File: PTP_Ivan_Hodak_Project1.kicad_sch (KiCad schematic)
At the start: 0 parts

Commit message: ispunjena sastavnica
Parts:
- added R1, R2: R_Small, symbol Device:R_Small
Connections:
- new net +3.3V: R2.1
- new net GND: R1.2
- new net U_izl: R1.1, R2.2
- no-connect marks 0 -> 1
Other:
- company: (none) -> TVZ
- title: (none) -> BCD Brojač

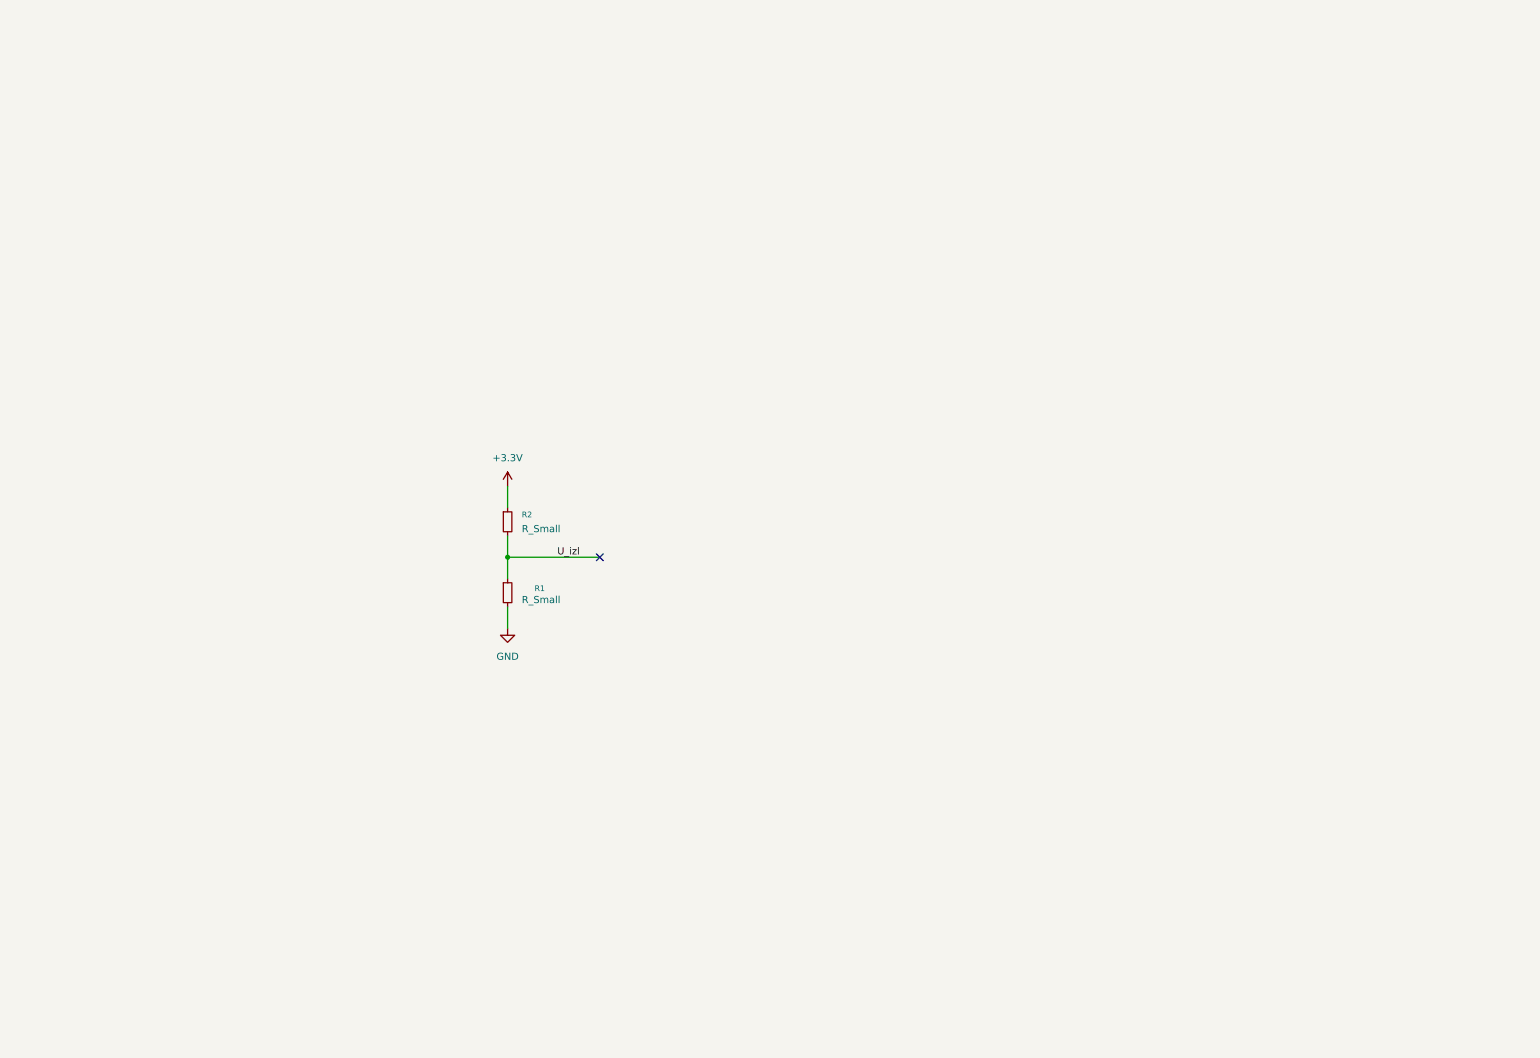
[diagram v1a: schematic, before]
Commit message: Dodali komponente
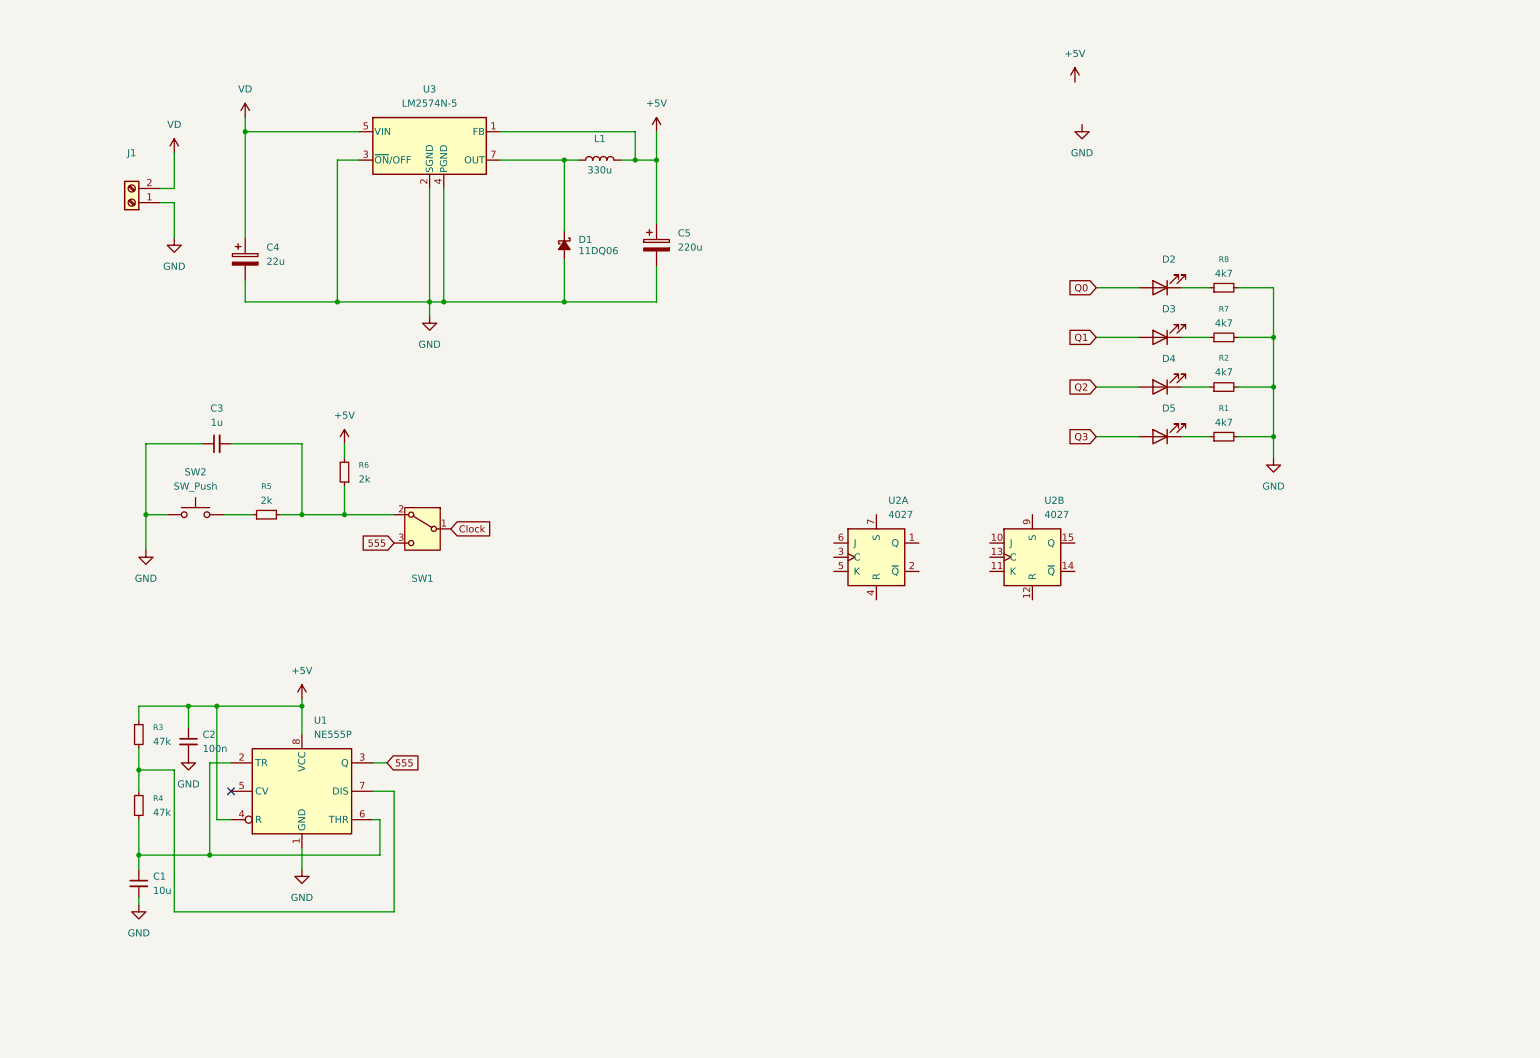
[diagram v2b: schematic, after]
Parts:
- added C1: 10u, symbol Device:C_Small
- added C2: 100n, symbol Device:C_Small
- added C3: 1u, symbol Device:C_Small
- added C4: 22u, symbol Device:C_Polarized
- added C5: 220u, symbol Device:C_Polarized
- added D1: 11DQ06, symbol Device:D_Schottky_Small_Filled
- added D2, D3, D4, D5: LED, symbol Device:LED
- added J1: ~, symbol Connector:Screw_Terminal_01x02
- added L1: 330u, symbol Device:L
- added R3, R4: 47k, symbol Device:R_Small
- added R5, R6: 2k, symbol Device:R_Small
- added R7, R8: 4k7, symbol Device:R_Small
- added SW1: SW_SPDT, symbol Switch:SW_SPDT
- added SW2: SW_Push, symbol Switch:SW_Push
- added U1: NE555P, Package_DIP:DIP-8_W7.62mm, symbol Timer:NE555P
- added U2: 4027, symbol 4xxx:4027
- added U3: LM2574N-5, Package_DIP:DIP-8_W7.62mm, symbol Regulator_Switching:LM2574N-5
- R1, R2: value R_Small -> 4k7
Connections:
- net GND: now also R2.2, C1.2, C2.2, C3.1, C4.2, C5.2, D1.2 (A), J1.1 (Pin_1), R7.2, R8.2, SW2.1, U1.1 (GND), U3.2 (SGND), U3.3 (~{ON}/OFF), U3.4 (PGND)
- net +3.3V: no longer names the net of R2.1
- net +3.3V: now also D4.1 (K)
- net U_izl: no longer names the net of R1.1
- net U_izl: now also D5.1 (K); no longer R2.2
- new net: C3.2, R5.2, R6.1, SW1.2 (B)
- new net: D1.1 (K), L1.1, U3.7 (OUT)
- new net: C1.1, R4.2, U1.2 (TR), U1.6 (THR)
- new net: R3.2, R4.1, U1.7 (DIS)
- new net: D3.1 (K), R7.1
- new net: D2.1 (K), R8.1
- new net: R5.1, SW2.2
- new net +5V: C2.1, C5.1, L1.2, R3.1, R6.2, U1.4 (R), U1.8 (VCC), U3.1 (FB)
- new net 555: SW1.3 (C), U1.3 (Q)
- new net Clock: SW1.1 (A)
- new net Q0: D2.2 (A)
- new net Q1: D3.2 (A)
- new net Q2: D4.2 (A)
- new net Q3: D5.2 (A)
- new net VD: C4.1, J1.2 (Pin_2), U3.5 (VIN)

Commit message: LV3
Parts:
- added U6: 74LVC1G11, SOT23-6:SOT-23-6, symbol SN74LVC1G11:SN74LVC1G11
- renumbered R5 to R13, R6 to R7, SW2 to SW1, SW1 to SW2
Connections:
- net +5V: now also U6.5 (Vcc)
- net Clock: now also R7.1, U6.3 (B)
- net GND: now also U6.2 (GND)
- net Q1: now also U6.6 (C)
- net Q3: now also U6.1 (A)
- net at C3.2, R13.2, SW2.2 (B): no longer R7.1
- new net Reset: U6.4 (Y)
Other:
- moved on the sheet: R7, SW2

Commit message: LV3 overwrite
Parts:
- R7: value 2k -> 10k
- renumbered C4 to C1, C5 to C2, D2 to D1, D3 to D2, D4 to D3, D1 to D4, R8 to R1, R7 to R2, R2 to R3, R1 to R4, U3 to U1
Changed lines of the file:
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@@
 			)
 		)
-		(property "Value" "2k"
+		(property "Value" "10k"
 			(at 88.9 100.3299 0)
 			(effects
@@
 		(on_board yes)
 		(dnp no)
-		(property "Reference" "D1"
+		(property "Reference" "D4"
 			(at 114.3 54.3559 90)
 			(effects
@@
 			(project ""
 				(path "/27044ca4-d0f9-45b4-abc4-d126f8e30ea6"
-					(reference "D1")
+					(reference "D4")
 					(unit 1)
 				)
@@
 		(dnp no)
 		(fields_autoplaced yes)
-		(property "Reference" "D4"
+		(property "Reference" "D3"
 			(at 220.0275 74.93 0)
 			(effects
@@
 			(project "PTP_Ivan_Hodak_Project1"
 				(path "/27044ca4-d0f9-45b4-abc4-d126f8e30ea6"
-					(reference "D4")
+					(reference "D3")
 					(unit 1)
 				)
@@
 		(dnp no)
 		(fields_autoplaced yes)
-		(property "Reference" "D3"
+		(property "Reference" "D2"
 			(at 220.0275 66.04 0)
 			(effects
@@
 			(project ""
 				(path "/27044ca4-d0f9-45b4-abc4-d126f8e30ea6"
-					(reference "D3")
+					(reference "D2")
 					(unit 1)
 				)
@@
 		(dnp no)
 		(fields_autoplaced yes)
-		(property "Reference" "D2"
+		(property "Reference" "D1"
 			(at 220.0275 57.15 0)
 			(effects
@@
 			(project ""
 				(path "/27044ca4-d0f9-45b4-abc4-d126f8e30ea6"
-					(reference "D2")
+					(reference "D1")
 					(unit 1)
 				)
@@
 		(dnp no)
 		(fields_autoplaced yes)
-		(property "Reference" "R2"
-			(at 229.87 74.8087 90)
+		(property "Reference" "R3"
+			(at 229.87 74.93 90)
 			(effects
 				(font
@@
 		)
 		(property "Value" "4k7"
-			(at 229.87 77.3487 90)
+			(at 229.87 77.47 90)
 			(effects
 				(font
@@
 			(project "PTP_Ivan_Hodak_Project1"
 				(path "/27044ca4-d0f9-45b4-abc4-d126f8e30ea6"
-					(reference "R2")
+					(reference "R3")
 					(unit 1)
 				)
@@
 		(dnp no)
 		(fields_autoplaced yes)
-		(property "Reference" "U3"
+		(property "Reference" "U1"
 			(at 87.63 26.67 0)
 			(effects
@@
 			(project ""
 				(path "/27044ca4-d0f9-45b4-abc4-d126f8e30ea6"
-					(reference "U3")
+					(reference "U1")
 					(unit 1)
 				)
@@
 		(dnp no)
 		(fields_autoplaced yes)
-		(property "Reference" "R1"
+		(property "Reference" "R4"
 			(at 229.87 83.82 90)
 			(effects
@@
 			(project ""
 				(path "/27044ca4-d0f9-45b4-abc4-d126f8e30ea6"
-					(reference "R1")
+					(reference "R4")
 					(unit 1)
 				)
@@
 		(dnp no)
 		(fields_autoplaced yes)
-		(property "Reference" "C5"
+		(property "Reference" "C2"
 			(at 132.08 52.4509 0)
 			(effects
@@
 			(project ""
 				(path "/27044ca4-d0f9-45b4-abc4-d126f8e30ea6"
-					(reference "C5")
+					(reference "C2")
 					(unit 1)
 				)
@@
 		(dnp no)
 		(fields_autoplaced yes)
-		(property "Reference" "R8"
+		(property "Reference" "R1"
 			(at 229.87 57.15 90)
 			(effects
@@
 			(project "PTP_Ivan_Hodak_Project1"
 				(path "/27044ca4-d0f9-45b4-abc4-d126f8e30ea6"
-					(reference "R8")
+					(reference "R1")
 					(unit 1)
 				)
@@
 		(dnp no)
 		(fields_autoplaced yes)
-		(property "Reference" "R7"
+		(property "Reference" "R2"
 			(at 229.87 66.04 90)
 			(effects
@@
 			(project "PTP_Ivan_Hodak_Project1"
 				(path "/27044ca4-d0f9-45b4-abc4-d126f8e30ea6"
-					(reference "R7")
+					(reference "R2")
 					(unit 1)
 				)
@@
 		(dnp no)
 		(fields_autoplaced yes)
-		(property "Reference" "C4"
+		(property "Reference" "C1"
 			(at 58.42 54.9909 0)
 			(effects
@@
 			(project ""
 				(path "/27044ca4-d0f9-45b4-abc4-d126f8e30ea6"
-					(reference "C4")
-					(unit 1)
-				)
+					(reference "C1")
+					(unit 1)
+				)

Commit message: Shema - gotova
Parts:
- added H1, H2, H3, H4: MountingHole, symbol Mechanical:MountingHole
- added R10, R11, R12, R15, R9: 10k, symbol Device:R_Small
- added R14, R16, R17, R18, R5, R6, R8: 2k, symbol Device:R_Small
- added unit 3 of U2
- added U3: 4027, symbol 4xxx:4027
- added U4: 74LS47, symbol 74xx:74LS47
- added U5: FYS-3911BUHR-21, Display_7Segment:HDSP-7401, symbol Display_Character:HDSP-7401
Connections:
- net +5V: now also R10.1, R11.1, R12.1, R15.2, R9.1, U2.16 (VDD), U3.16 (VDD), U4.16 (VCC), U5.1 (CA), U5.6 (CA)
- net Clock: now also U2.3 (C)
- net GND: now also U2.7 (S), U2.9 (S), U2.8 (VSS), U3.7 (S), U3.8 (VSS), U3.9 (S), U4.8 (GND)
- net Q0: now also U2.1 (Q), U2.13 (C), U4.7 (A)
- net Q1: now also U2.15 (Q), U3.3 (C), U4.1 (B)
- net Q2: now also U3.1 (Q), U3.13 (C), U4.2 (C)
- net Q3: now also U3.15 (Q), U4.6 (D)
- net Reset: now also U2.12 (R), U2.4 (R), U3.12 (R), U3.4 (R)
- net at U2.5 (K): now also U2.6 (J), R9.2
- net at U2.10 (J): now also U2.11 (K), R10.2
- new net: R11.2, U3.5 (K), U3.6 (J)
- new net: R5.1, U4.13 (a)
- new net: R5.2, U5.10 (A)
- new net: R14.1, U4.10 (d)
- new net: R8.1, U4.11 (c)
- new net: R6.1, U4.12 (b)
- new net: R18.1, U4.14 (g)
- new net: R17.1, U4.15 (f)
- new net: R15.1, U4.3 (LT), U4.4 (BI), U4.5 (RBI)
- new net: R16.1, U4.9 (e)
- new net: R8.2, U5.8 (C)
- new net: R17.2, U5.2 (F)
- new net: R18.2, U5.3 (G)
- new net: R6.2, U5.9 (B)
- new net: R12.2, U3.10 (J), U3.11 (K)
- new net: R16.2, U5.4 (E)
- new net: R14.2, U5.5 (D)
- no-connect marks 1 -> 6
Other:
- note added: "555 timer"
- note added: "JK bistabili"
- note added: "LED diode"
- note added: "Montažne rupe"
- note added: "Napajanje"
- note added: "Napajanje bistabila"
- note added: "Reset brojač"
- note added: "Tipkalo i ulaz radnog takta"
- moved on the sheet: C1, C2, C3, D1, D2, D3, D4, D5, J1, L1, R1, R13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

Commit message: Shema - Citanje iz Excela
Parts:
- D1, D2, D3, D5: footprint (none) -> LED_THT:LED_D5.0mm
- R14, R16, R17, R18, R5, R6: footprint (none) -> Resistor_SMD:R_1206_3216Metric_Pad1.30x1.75mm_HandSolder; Manufacturer (none) -> ROYALOHM; Manufacturer part number (none) -> 1206S4F2001T5E
- R8: footprint (none) -> Resistor_SMD:R_1206_3216Metric_Pad1.30x1.75mm_HandSolder; Manufacturer (none) -> ROYAMOHM; Manufacturer part number (none) -> 1206S4F2001T5E
- U2, U3: footprint (none) -> Package_DIP:DIP-16_W7.62mm_Socket_LongPads; Manufacturer (none) -> RENESAS; Manufacturer part number (none) -> CD4027BMS
- U4: footprint (none) -> Package_DIP:DIP-16_W7.62mm_Socket_LongPads; Manufacturer (none) -> TEXAS INSTRUMENTS; Manufacturer oart number (none) -> SN74LS47N
- U5: Manufacturer (none) -> FORYARD; Manufacturer part number (none) -> FYS-3911BUHR-21

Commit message: Shema
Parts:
- renumbered C2 to C4, C1 to C5, R3 to R19, R4 to R20, U1 to U0
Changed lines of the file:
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@@
 	)
 	(junction
+		(at 25.4 38.1)
+		(diameter 0)
+		(color 0 0 0 0)
+	)
+	(junction
 		(at 73.66 58.42)
 		(diameter 0)
@@
 	(wire
 		(pts
+			(xy 31.75 38.1) (xy 25.4 38.1)
+		)
+		(stroke
+			(width 0)
+			(type default)
+		)
+	)
+	(wire
+		(pts
 			(xy 33.02 87.63) (xy 22.86 87.63)
 		)
@@
 	(wire
 		(pts
+			(xy 31.75 36.83) (xy 31.75 38.1)
+		)
+		(stroke
+			(width 0)
+			(type default)
+		)
+	)
+	(wire
+		(pts
 			(xy 243.84 100.33) (xy 243.84 111.76)
 		)
@@
 	(wire
 		(pts
-			(xy 38.1 27.94) (xy 38.1 25.4)
+			(xy 38.1 27.94) (xy 38.1 21.59)
 		)
 		(stroke
@@
 		(dnp no)
 		(fields_autoplaced yes)
-		(property "Reference" "U1"
+		(property "Reference" "U0"
 			(at 55.4833 148.59 0)
 			(effects
@@
 			(project ""
 				(path "/27044ca4-d0f9-45b4-abc4-d126f8e30ea6"
-					(reference "U1")
+					(reference "U0")
 					(unit 1)
 				)
@@
 		(dnp no)
 		(fields_autoplaced yes)
-		(property "Reference" "C2"
+		(property "Reference" "C4"
 			(at 35.56 151.1362 0)
 			(effects
@@
 			(project ""
 				(path "/27044ca4-d0f9-45b4-abc4-d126f8e30ea6"
-					(reference "C2")
+					(reference "C4")
 					(unit 1)
 				)
@@
 	(symbol
 		(lib_id "power:VD")
-		(at 38.1 25.4 0)
+		(at 38.1 21.59 0)
 		(unit 1)
 		(exclude_from_sim no)
@@
 		(fields_autoplaced yes)
 		(property "Reference" "#PWR012"
-			(at 38.1 29.21 0)
+			(at 38.1 25.4 0)
 			(effects
 				(font
@@
 		)
 		(property "Value" "VD"
-			(at 38.1 20.32 0)
+			(at 38.1 16.51 0)
 			(effects
 				(font
@@
 		)
 		(property "Footprint" ""
-			(at 38.1 25.4 0)
+			(at 38.1 21.59 0)
 			(effects
 				(font
@@
 		)
 		(property "Datasheet" ""
-			(at 38.1 25.4 0)
+			(at 38.1 21.59 0)
 			(effects
 				(font
@@
 		)
 		(property "Description" "Power symbol creates a global label with name \"VD\""
-			(at 38.1 25.4 0)
+			(at 38.1 21.59 0)
 			(effects
 				(font
@@
 		(dnp no)
 		(fields_autoplaced yes)
-		(property "Reference" "C1"
+		(property "Reference" "C5"
 			(at 26.67 176.5362 0)
 			(effects
@@
 			(project ""
 				(path "/27044ca4-d0f9-45b4-abc4-d126f8e30ea6"
-					(reference "C1")
+					(reference "C5")
 					(unit 1)
 				)
@@
 	)
 	(symbol
+		(lib_id "power:PWR_FLAG")
+		(at 31.75 36.83 0)
+		(unit 1)
+		(exclude_from_sim no)
+		(in_bom yes)
+		(on_board yes)
+		(dnp no)
+		(fields_autoplaced yes)
+		(property "Reference" "#FLG02"
+			(at 31.75 34.925 0)
+			(effects
+				(font
+					(size 1.27 1.27)
+				)
+				(hide yes)
+			)
+		)
+		(property "Value" "PWR_FLAG"
+			(at 31.75 31.75 0)
+			(effects
+				(font
+					(size 1.27 1.27)
+				)
+			)
+		)
+		(property "Footprint" ""
+			(at 31.75 36.83 0)
+			(effects
+				(font
+					(size 1.27 1.27)
+				)
+				(hide yes)
+			)
+		)
+		(property "Datasheet" "~"
+			(at 31.75 36.83 0)
+			(effects
+				(font
+					(size 1.27 1.27)
+				)
+				(hide yes)
+			)
+		)
+		(property "Description" "Special symbol for telling ERC where power comes from"
+			(at 31.75 36.83 0)
+			(effects
+				(font
+					(size 1.27 1.27)
+				)
+				(hide yes)
+			)
+		)
+		(pin "1"
+		)
+		(instances
+			(project ""
+				(path "/27044ca4-d0f9-45b4-abc4-d126f8e30ea6"
+					(reference "#FLG02")
+					(unit 1)
+				)
+			)
+		)
+	)
+	(symbol
 		(lib_id "Device:R_Small")
 		(at 252.73 73.66 90)
@@
 		(dnp no)
 		(fields_autoplaced yes)
-		(property "Reference" "R4"
+		(property "Reference" "R20"
 			(at 26.67 162.5599 0)
 			(effects
@@
 			(project "PTP_Ivan_Hodak_Project1"
 				(path "/27044ca4-d0f9-45b4-abc4-d126f8e30ea6"
-					(reference "R4")
+					(reference "R20")
 					(unit 1)
 				)
@@
 		(dnp no)
 		(fields_autoplaced yes)
-		(property "Reference" "R3"
+		(property "Reference" "R19"
 			(at 26.67 149.8599 0)
 			(effects
@@
 			(project ""
 				(path "/27044ca4-d0f9-45b4-abc4-d126f8e30ea6"
-					(reference "R3")
+					(reference "R19")
 					(unit 1)
 				)

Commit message: LV6
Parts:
- C1: footprint (none) -> Capacitor_THT:CP_Radial_D5.0mm_P2.00mm; Manufacturer (none) -> AISHI; Manufacturer part number (none) -> EWH1EM220D11OT
- C2: footprint (none) -> Capacitor_THT:CP_Radial_D5.0mm_P2.00mm; Manufacturer (none) -> SAMWHA; Manufacturer part number (none) -> RD1A227M05011BB
- C3: footprint (none) -> Capacitor_SMD:C_1206_3216Metric_Pad1.33x1.80mm_HandSolder; Manufacturer (none) -> SAMSUNG; Manufacturer part number (none) -> CL31B105KBHNNNE
- C4: footprint (none) -> Capacitor_SMD:C_1206_3216Metric_Pad1.33x1.80mm_HandSolder; Manufacturer (none) -> SAMSUNG; Manufacturer part number (none) -> CL31B104KBCNNNC
- C5: footprint (none) -> Capacitor_SMD:C_1206_3216Metric_Pad1.33x1.80mm_HandSolder; Manufacturer (none) -> SAMSUNG; Manufacturer part number (none) -> CL31A106KBHNNNE
- D4: footprint (none) -> Diode_THT:D_DO-41_SOD81_P12.70mm_Horizontal; Manufacturer (none) -> SMC DIODE SOLUTIONS; Manufacturer part number (none) -> 11DQ06TA
- H1, H2, H3, H4: footprint (none) -> MountingHole:MountingHole_5.5mm
- J1: footprint (none) -> TerminalBlock_MetzConnect:TerminalBlock_MetzConnect_Type011_RT05502HBLC_1x02_P5.00mm_Horizontal; Manufacturer (none) -> DEGSON ELECTRONICS; Manufacturer part number (none) -> DG301-5.0-02P-12-00A(H)
- L1: footprint (none) -> Inductor_THT:L_Radial_D7.2mm_P3.00mm_Murata_1700; Manufacturer (none) -> FERROCORE; Manufacturer part number (none) -> COIL0608-0.33
- R1, R2, R3, R4: footprint (none) -> Resistor_THT:R_Axial_DIN0207_L6.3mm_D2.5mm_P10.16mm_Horizontal
- R10, R11, R12, R15, R7, R9: footprint (none) -> Resistor_SMD:R_1206_3216Metric_Pad1.30x1.75mm_HandSolder
- R19, R20: footprint (none) -> Resistor_SMD:R_1206_3216Metric_Pad1.30x1.75mm_HandSolder; Manufacturer (none) -> ROYALOHM; Manufacturer part number (none) -> 1206S4J0473T5E
- SW1: footprint (none) -> Button_Switch_THT:SW_PUSH_6mm_H4.3mm; Manufacturer (none) -> microswitch TACT; Manufacturer part number (none) -> TACT-64N-F
- SW2: footprint (none) -> Button_Switch_THT:SW_Slide_SPDT_Straight_CK_OS102011MS2Q; Manufacturer (none) -> C&K; Manufacturer part number (none) -> OS102011MS2QN1C
- U0: Manufacturer (none) -> TEXAS INSTRUMENTS; Manufacturer part number (none) -> NE555P
- U1: Manufacturer part number (none) -> LM2574N-5G; Manufcaturer (none) -> ONSEMI
- U4: Manufacturer oart number SN74LS47N -> (none)
- U6: Manufacturer (none) -> TEXAS INSTRUMENTS; Manufacturer part number (none) -> SN74LVC1G11DBVR
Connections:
- net Clock: now also SW2.2 (B); no longer SW2.1 (A)
- net at C3.2, R13.2: now also SW2.1 (A); no longer SW2.2 (B)
